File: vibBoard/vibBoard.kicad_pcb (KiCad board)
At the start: 2 copper layers, 45.7 x 45.7 mm, 47 parts, among them J1 CAN Bus Connector, J2 Programming Header, J3 Micro_SD_Card, J4 THMS Connector, J5 PT 1 Connector, J6 PT 2 Connector, U1 SPX3819M5-L-3-3, U2 INA180, U3 AIS3624DQTR, U4 PIC18F26K83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

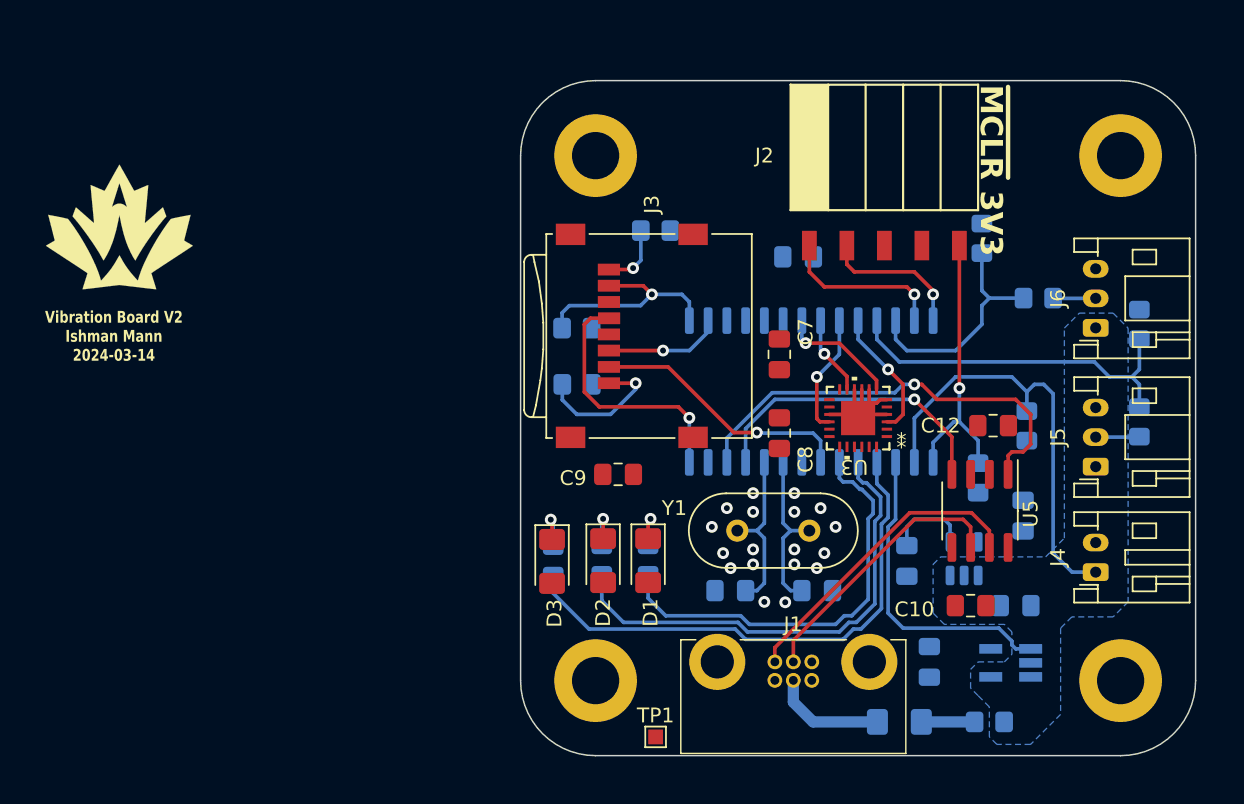
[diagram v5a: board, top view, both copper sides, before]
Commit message: everything routed except gnd
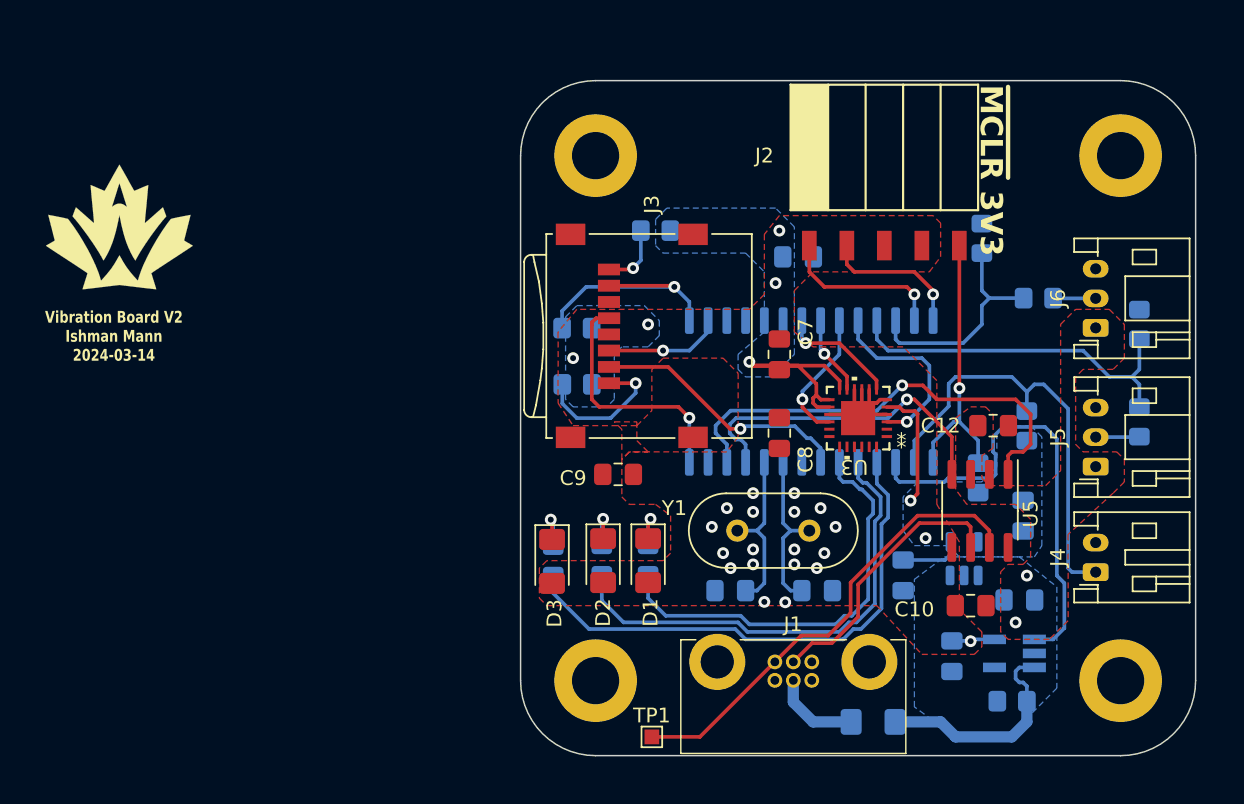
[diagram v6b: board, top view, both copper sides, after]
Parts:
- moved R1 2.08 mm to (161.6, 134.7), turned to 0 degrees
- moved F1 1.78 mm to (152.1, 136.1)
- moved C4 1.57 mm to (157.5, 131.7)
- moved C2 1.01 mm to (154.2, 126.2)
- moved U2 0.69 mm to (161.7, 131.5)
- moved C1 0.46 mm to (162.1, 127.9)
- moved TP1 0.25 mm to (137.2, 137.2)
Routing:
- net +3.3V: track 0.00 -> 26.9 mm, vias 0 -> 8
- net Net-(U2-IN+): track 3.61 -> 15.0 mm
- net /CANH: track 20.9 -> 31.8 mm
- net /CURR_SENSE: track 21.2 -> 31.1 mm
- net /AIS3624DQTR_IOC: track 8.92 -> 12.6 mm
- net /CANTX: track 20.9 -> 22.8 mm
- net /MICRO_SD_SDI: track 14.8 -> 16.6 mm
- net Net-(J1-Pin_5): track 7.72 -> 5.95 mm
- net /CANRX: track 29.7 -> 31.2 mm
- net Net-(U1-BP): track 5.70 -> 4.21 mm
- net /AIS3624DQTR_SDA: track 8.21 -> 9.15 mm
- net /MICRO_SD_SCK: track 17.3 -> 16.6 mm
- net Net-(J3-DAT2): track 9.35 -> 9.86 mm
- net +5V: vias 0 -> 2
- added copper zone on B.Cu, net +3.3V
- added copper zone on F.Cu, net +3.3V
- added copper zone on F.Cu, net +5V

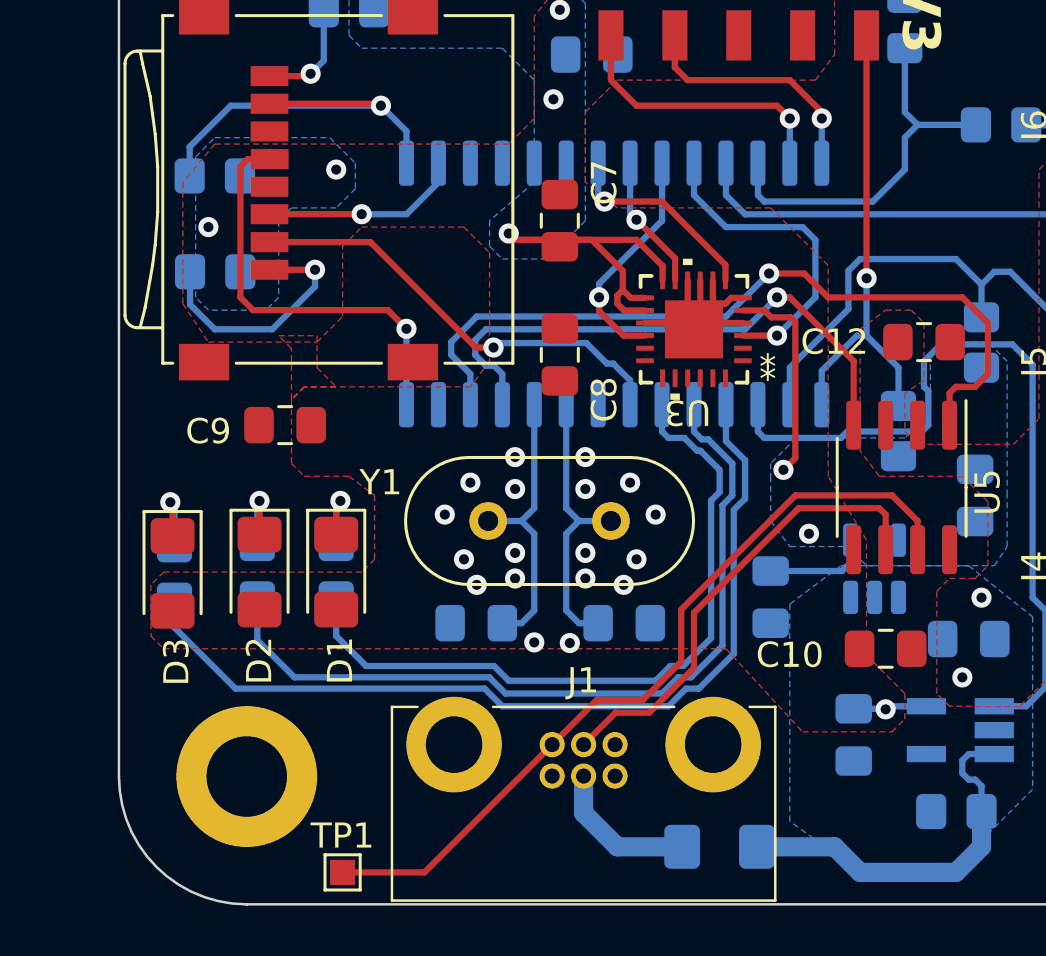
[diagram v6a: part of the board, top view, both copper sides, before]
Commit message: oscillator gnd added
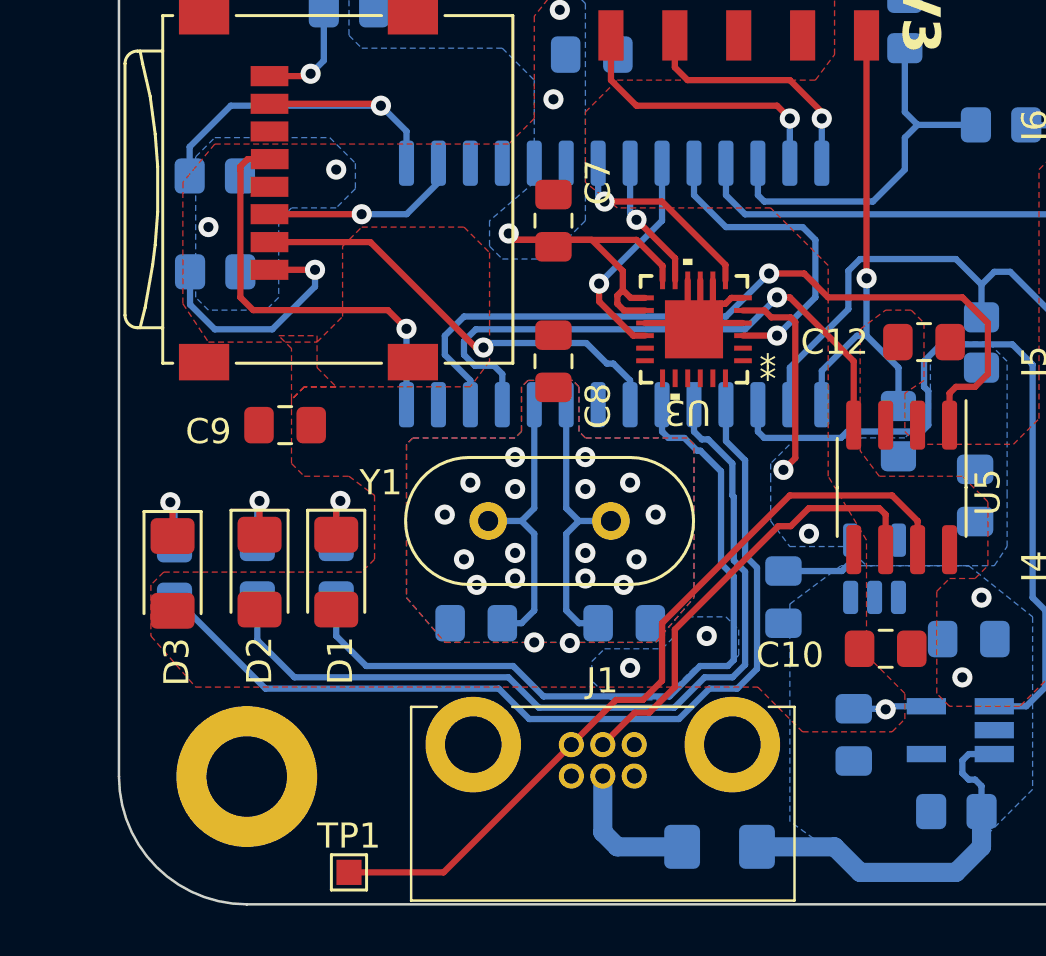
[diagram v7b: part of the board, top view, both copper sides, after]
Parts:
- moved J1 0.76 mm to (147.5, 132.1)
- moved C2 0.51 mm to (154.7, 126.2)
- moved C8 0.36 mm to (145.5, 116.8)
- moved C7 0.25 mm to (145.5, 111.3)
- moved TP1 0.25 mm to (137.4, 137.2)
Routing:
- net Net-(U4-RA4): track 28.7 -> 30.8 mm
- net Net-(U4-RA3): track 32.4 -> 34.3 mm
- net Net-(U4-RA2): track 36.0 -> 37.0 mm
- net /CANTX: track 22.8 -> 23.7 mm
- net /CANL: track 18.7 -> 18.0 mm
- net /CANRX: track 31.2 -> 31.7 mm
- net Net-(U1-BP): track 4.21 -> 3.70 mm
- net +3.3V: vias 8 -> 10
- added copper zone on B.Cu, net GND
- added copper zone on F.Cu, net GND

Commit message: more gnd added
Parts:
- moved C8 0.76 mm to (145.5, 117.6)
- moved D3 0.59 mm to (131.0, 125.2)
- moved R7 0.59 mm to (131.1, 125.2)
- moved R3 0.51 mm to (132.1, 110.0)
- moved D2 0.25 mm to (134.1, 125.2)
- moved R6 0.25 mm to (134.0, 125.2)
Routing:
- net GND: track 12.2 -> 25.9 mm, vias 18 -> 73
- net +3.3V: track 26.9 -> 23.8 mm, vias 10 -> 8
- net /AIS3624DQTR_IOC: track 12.6 -> 15.3 mm
- net /CANTX: track 23.7 -> 26.0 mm
- net /AIS3624DQTR_INT: track 8.09 -> 9.44 mm
- net /AIS3624DQTR_SDA: track 8.92 -> 10.0 mm
- net /CANRX: track 31.7 -> 32.6 mm
- net /PT_2_SENSE: track 15.3 -> 14.5 mm
- net /THMS_SENSE: track 30.0 -> 30.7 mm
- net Net-(U2-IN+): track 15.0 -> 14.4 mm
- net /ICSPCLK: track 11.3 -> 10.7 mm
